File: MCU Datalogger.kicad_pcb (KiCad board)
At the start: 2 copper layers, 29 parts, among them J1 Conn_01x04_Pin, J2 Conn_01x04_Pin, J3 Conn_01x09_Pin, J4 Conn_02x03_Odd_Even, U1 24LC1025, U2 24LC1025, U3 DS1337S_, U4 ATMEGA328P-AU, Y1 16 MHz, Y2 32.768kHz

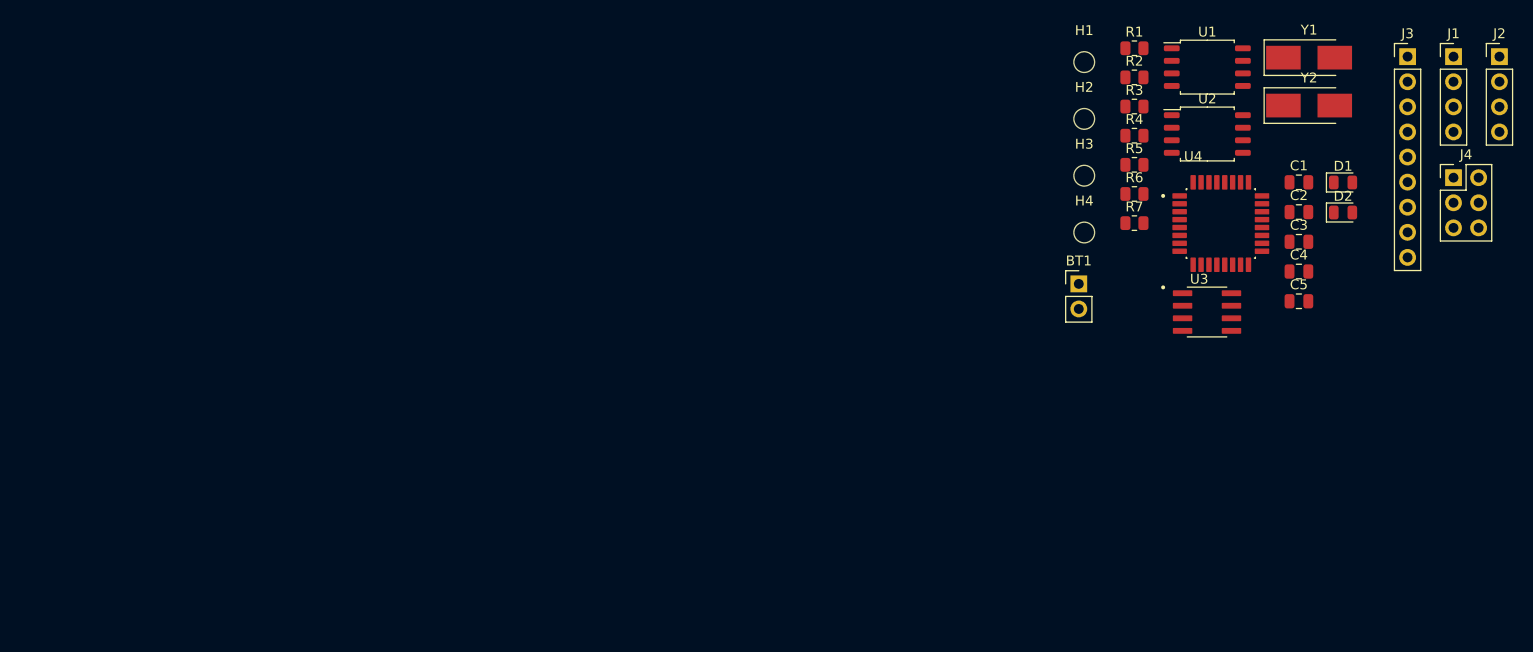
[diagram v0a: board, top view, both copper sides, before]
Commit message: completed placement of footprints
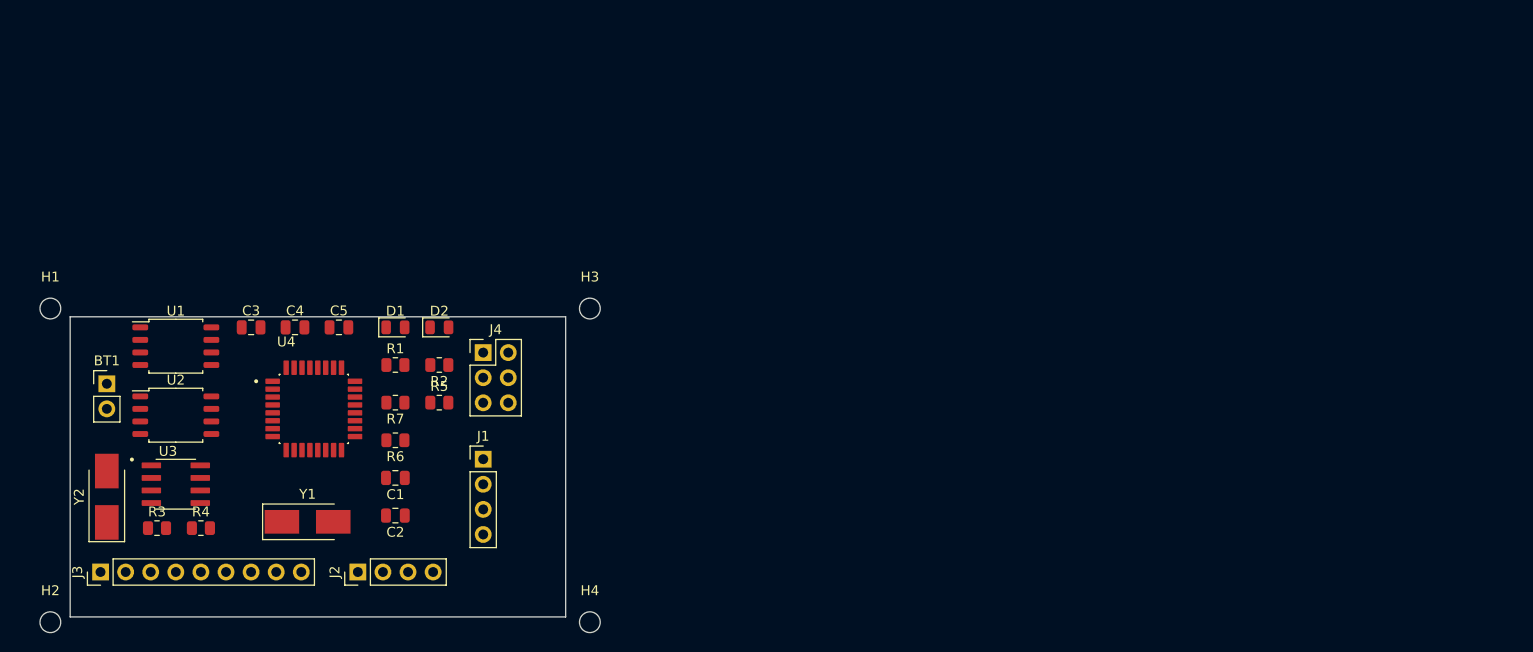
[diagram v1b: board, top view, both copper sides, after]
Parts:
- C2, C4: value 0.1u -> 100n
- moved J3 142.2 mm to (132.1, 76.2), turned to 90 degrees
- moved Y2 128.0 mm to (132.7, 68.6), turned to 90 degrees
- moved J2 126.8 mm to (158.1, 76.2), turned to 90 degrees
- moved H2 116.4 mm to (127.0, 81.3)
- moved Y1 111.7 mm to (153.0, 71.1)
- moved U2 108.2 mm to (139.7, 60.3)
- moved U1 108.2 mm to (139.7, 53.3)
- moved R3 107.7 mm to (137.8, 71.8)
- moved H1 107.6 mm to (127.0, 49.5)
- moved C3 106.4 mm to (147.3, 51.4)
- moved J1 106.3 mm to (170.8, 64.8)
- moved U3 105.8 mm to (139.7, 67.3)
- moved R4 102.5 mm to (142.2, 71.8)
- moved C4 101.8 mm to (151.8, 51.4)
- moved J4 99.8 mm to (170.8, 54.0)
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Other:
- board outline added: 50.2 x 30.4 mm

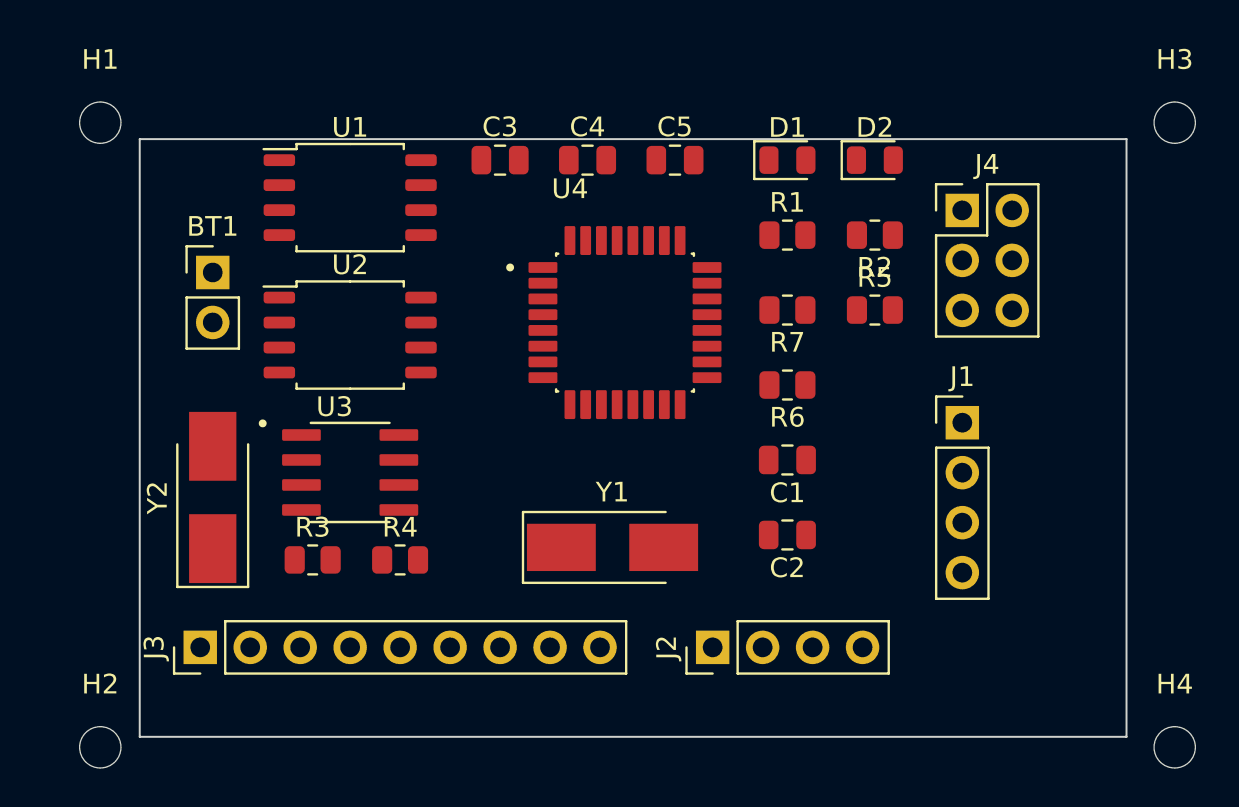
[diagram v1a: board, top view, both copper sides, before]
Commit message: Routing completed, PWR zones added, DRC checked
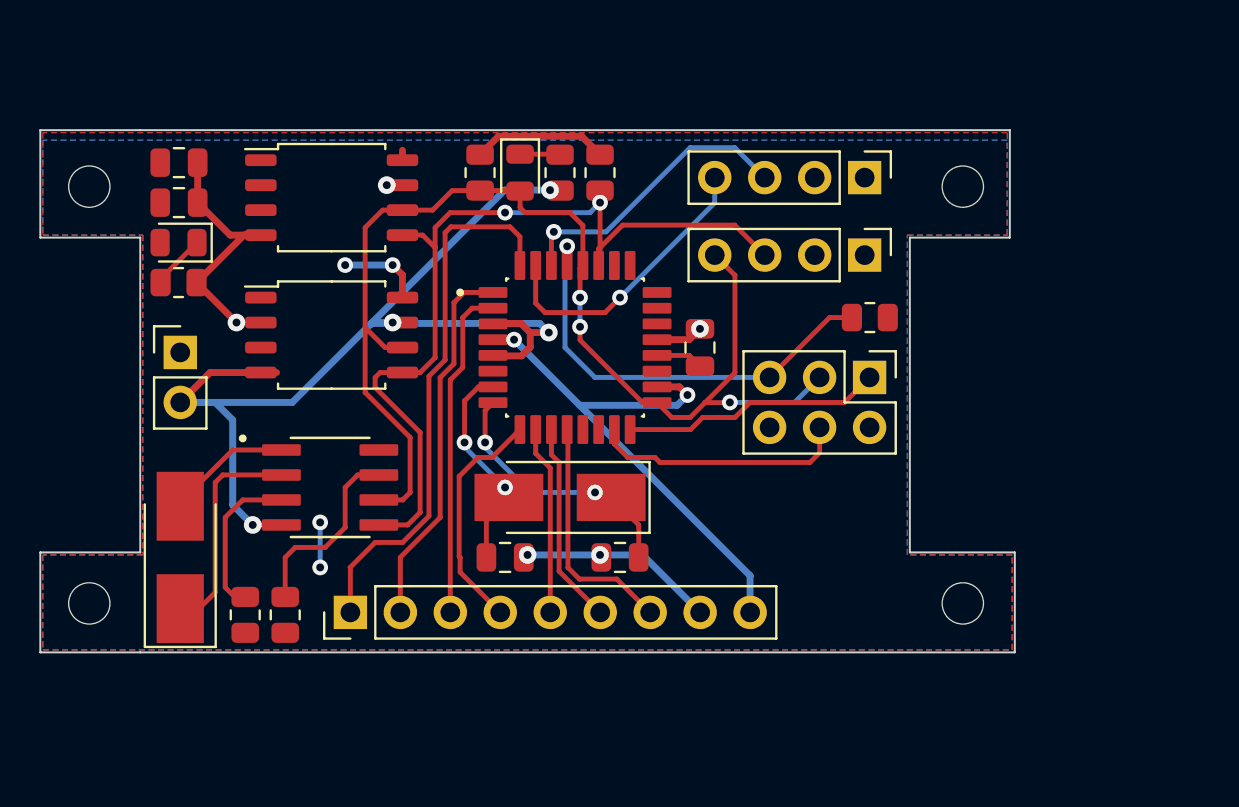
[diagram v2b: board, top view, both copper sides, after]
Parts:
- moved H3 60.3 mm to (126.4, 74.0)
- moved H2 52.3 mm to (170.8, 52.8)
- moved D1 31.2 mm to (131.0, 55.6), turned to 180 degrees
- moved R1 31.0 mm to (131.0, 57.7)
- moved C5 25.3 mm to (131.0, 53.6)
- moved J2 25.1 mm to (165.9, 52.3), turned to -90 degrees
- moved C3 21.1 mm to (153.4, 71.6)
- moved C4 20.8 mm to (131.0, 51.6), turned to 180 degrees
- moved R6 19.0 mm to (146.3, 52.1), turned to -90 degrees
- moved D2 18.0 mm to (148.3, 52.1), turned to -90 degrees
- moved R2 16.3 mm to (150.4, 52.1), turned to 90 degrees
- moved C1 15.2 mm to (147.6, 71.6)
- moved H4 13.0 mm to (170.8, 74.0)
- moved R7 11.8 mm to (152.4, 52.1), turned to -90 degrees
- moved C2 10.5 mm to (157.5, 61.0), turned to -90 degrees
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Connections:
- net Net-(U3-SQW/~INT) renamed /SQW
- net Net-(U3-~{INTA}) renamed /~{INTA}
- net Net-(U4-AREF) renamed /AREF
- BT1 pad 1: Net-(BT1-+) -> /Vcc
- C5 pad 1: Net-(BT1-+) -> /Vcc
- D1 pad 2: Net-(BT1-+) -> /Vcc
- U4 pad 18: Net-(BT1-+) -> /Vcc
- U4 pad 4: Net-(BT1-+) -> /Vcc
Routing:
- net GND: track 0.00 -> 83.0 mm, vias 0 -> 9
- net /SCK: track 0.00 -> 60.6 mm, vias 0 -> 3
- net /SDA: track 0.00 -> 45.6 mm, vias 0 -> 2
- net /Vcc: track 0.00 -> 39.5 mm, vias 0 -> 4
- net /D2: track 0.00 -> 27.7 mm
- net /RESET: track 0.00 -> 22.0 mm, vias 0 -> 1
- net /D3: track 0.00 -> 19.1 mm
- net /D4: track 0.00 -> 17.0 mm
- net /RX: track 0.00 -> 14.9 mm, vias 0 -> 1
- net /TX: track 0.00 -> 14.8 mm, vias 0 -> 1
- net Net-(U4-PB7): track 0.00 -> 13.5 mm, vias 0 -> 2
- net /MISO: track 0.00 -> 13.3 mm
- net /MOSI: track 0.00 -> 13.0 mm
- net /D8: track 0.00 -> 12.2 mm
- net /D5: track 0.00 -> 11.9 mm
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- added copper zone on F.Cu, net /Vcc
- added copper zone on B.Cu, net GND
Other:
- board size 50.2 x 30.4 mm -> 49.5 x 26.5 mm
- board text added: "Afterall, there are some clearence violations that must be corrected"
- board text added: "CORRECTED"
- board text added: "Unfortunately Vcc label is not defined as POWER net class so that Vcc track width was set as default (0.25mm). After the DRC process, the net class definitions checked and reorganized. Labels that entered by users should write with {dblquote}/{dblquote} prefix. For example /Vcc ."

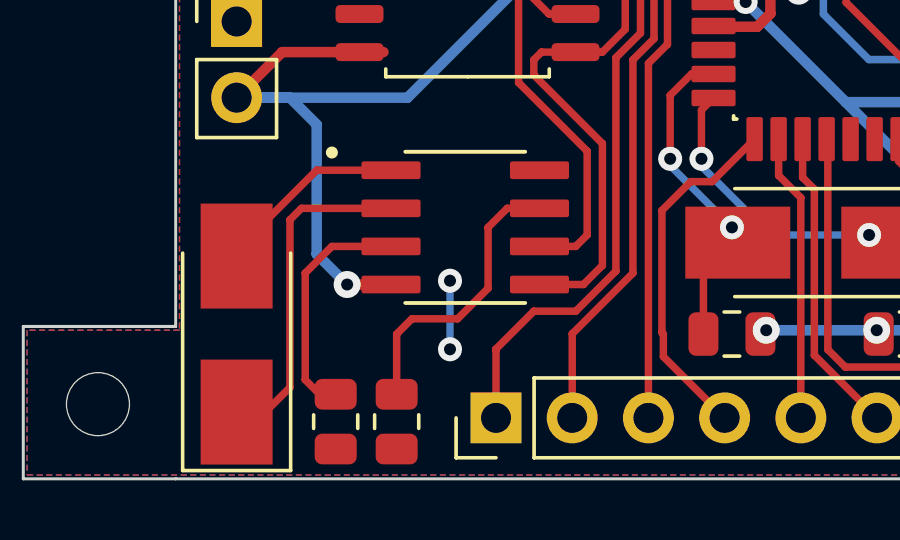
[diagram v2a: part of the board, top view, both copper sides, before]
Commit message: Routing completed, PWR zones added, DRC checked
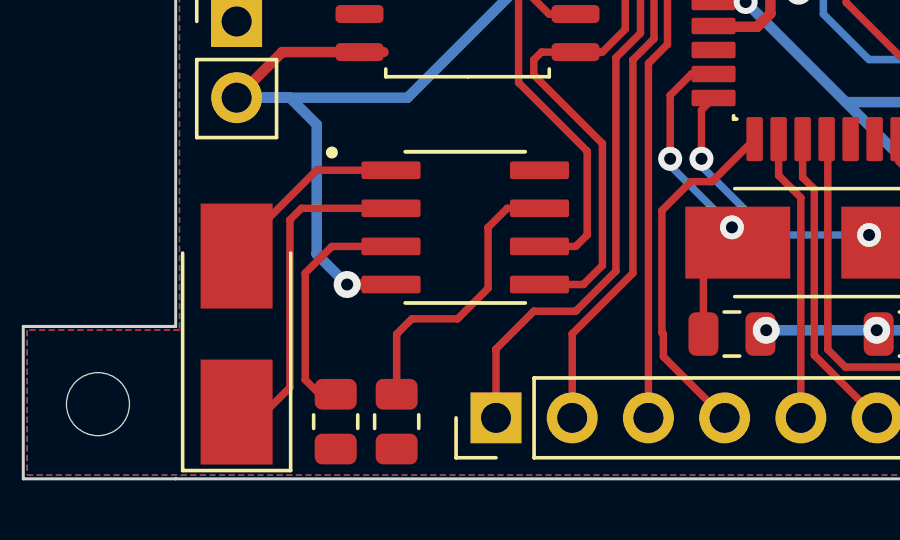
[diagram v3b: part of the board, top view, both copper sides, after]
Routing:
- net (no net): track 2.41 -> 0.00 mm, vias 2 -> 0
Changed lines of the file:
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@@
     (effects (font (size 2 2) (thickness 0.2) bold) (justify left bottom))
   )
-  (segment (start 138.176 72.263) (end 138.176 72.136) (width 0.25) (layer "F.Cu") (net 0))
-  (via (at 138.176 69.85) (size 0.8) (drill 0.4) (layers "F.Cu" "B.Cu") (net 0))
-  (via (at 138.176 72.136) (size 0.8) (drill 0.4) (layers "F.Cu" "B.Cu") (net 0))
-  (segment (start 138.176 72.136) (end 138.176 69.85) (width 0.25) (layer "B.Cu") (net 0))
   (segment (start 142.36 59.69) (end 141.859 59.69) (width 0.35) (layer "F.Cu") (net 1))
   (segment (start 134.3035 55.245) (end 131.8905 57.658) (width 0.35) (layer "F.Cu") (net 1))

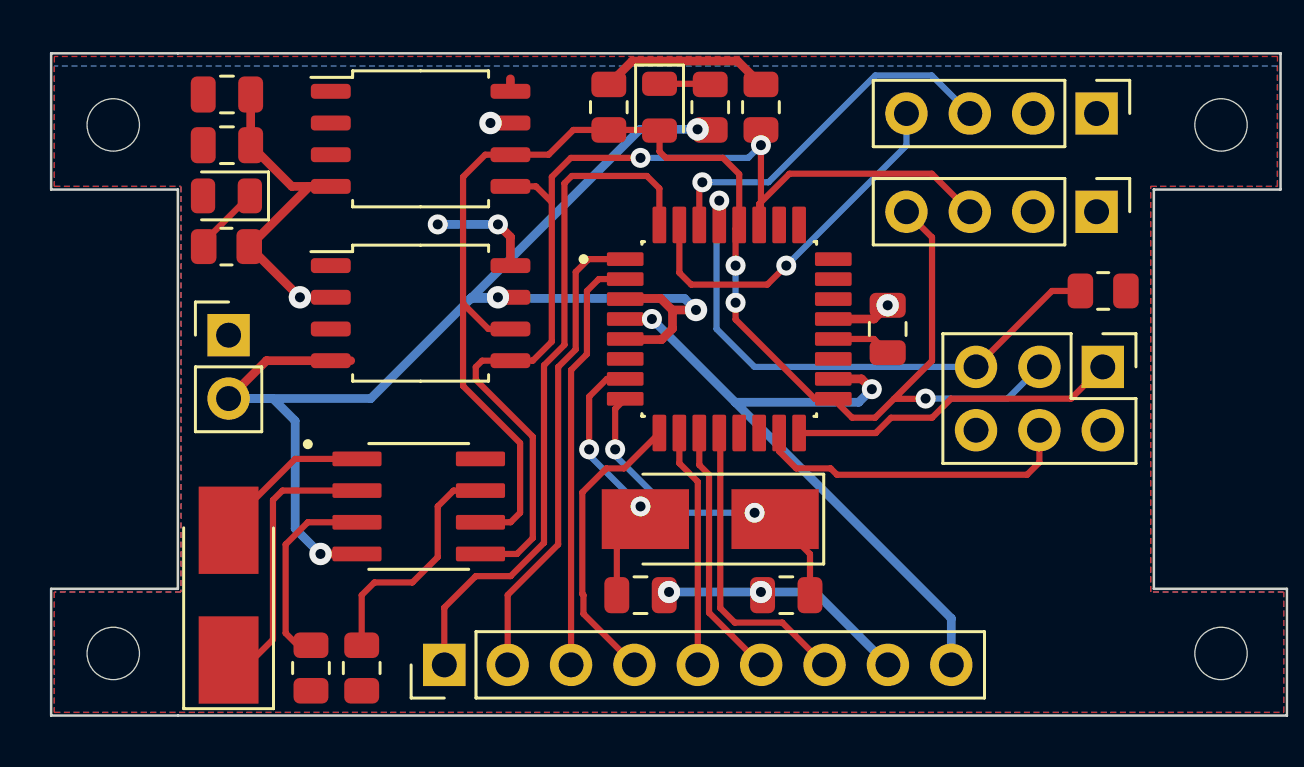
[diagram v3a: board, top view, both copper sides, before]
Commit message: Silkscreen texts added and adjusted
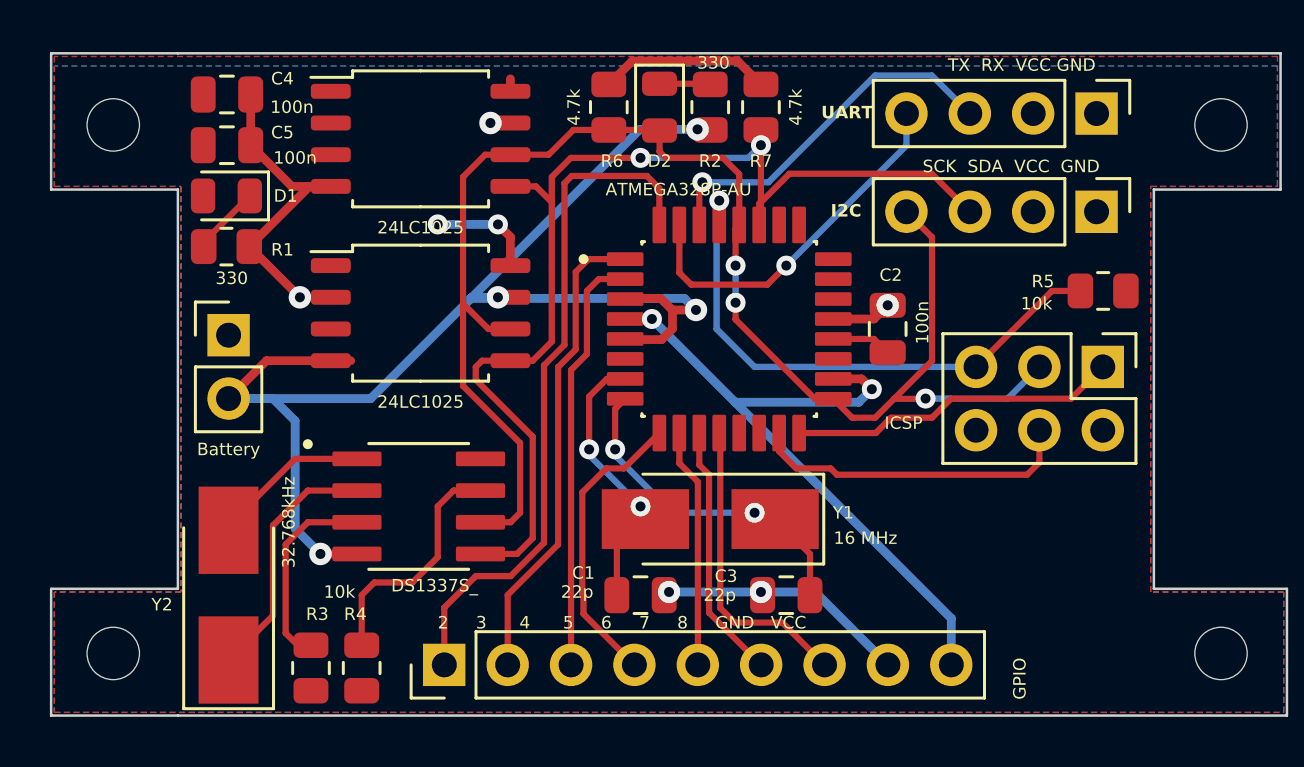
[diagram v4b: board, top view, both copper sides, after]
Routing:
- net Net-(U3-X2): track 11.2 -> 10.1 mm
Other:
- board text added: "2 3 4 5 6 7 8 GND VCC"
- board text added: "GPIO"
- board text added: "I2C"
- board text added: "ICSP"
- board text added: "SCK SDA VCC GND"
- board text added: "TX RX VCC GND"
- board text added: "UART"
